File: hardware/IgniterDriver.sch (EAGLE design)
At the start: 22 parts, among them IC1 ATMEGA48/88/168-AU, Q1 FDD4141TO252, Q2 IRLML5203, Q4 16MHz, U2 MCP25625-E/SS

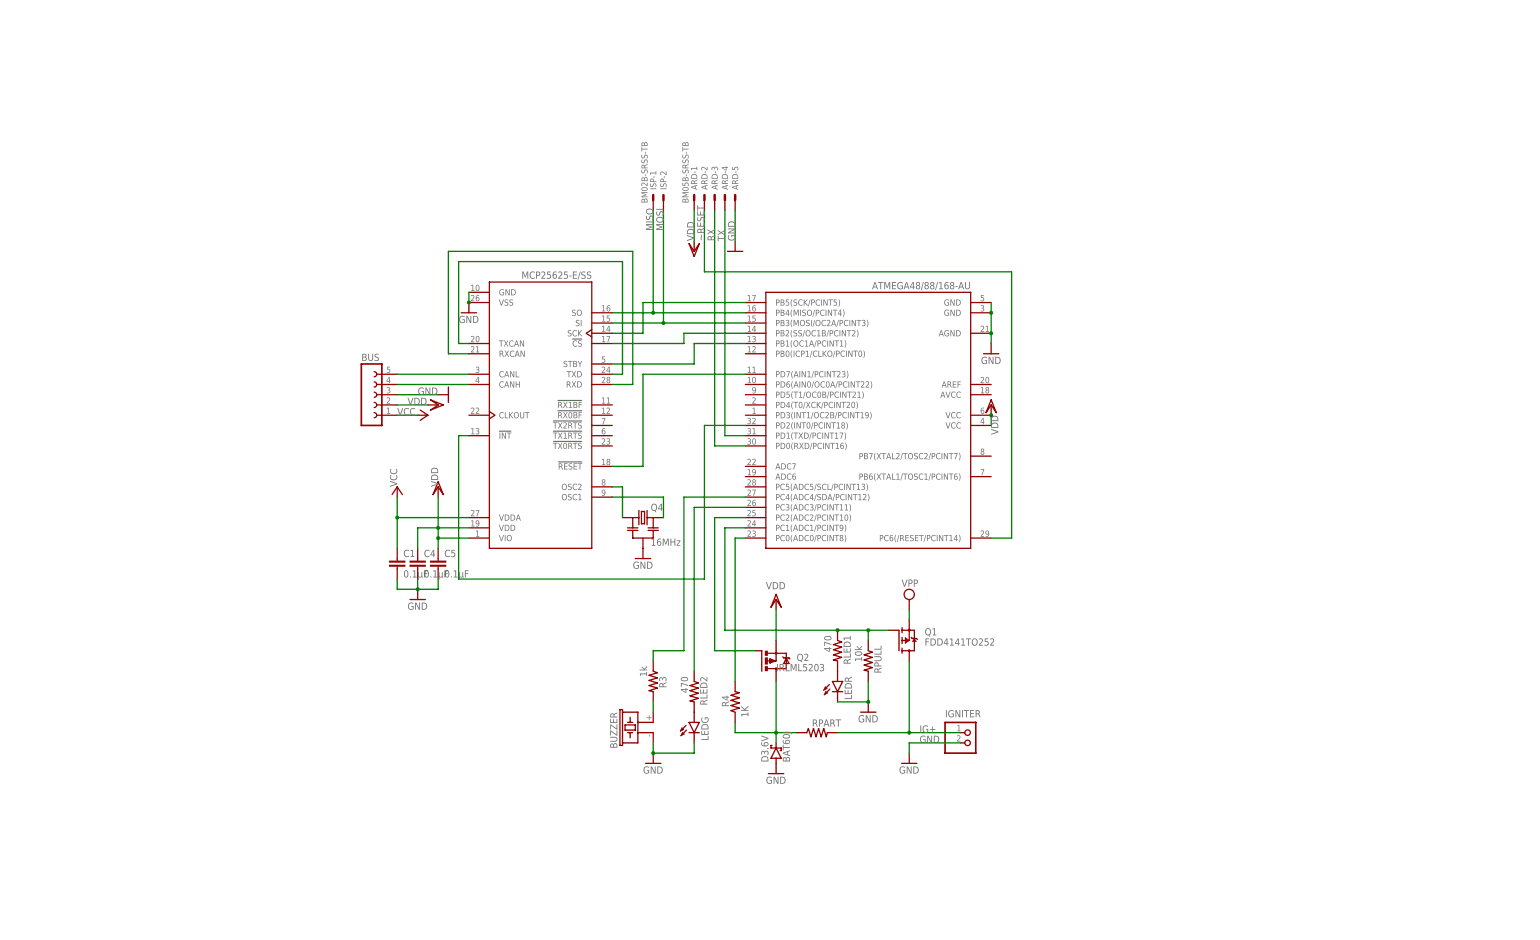
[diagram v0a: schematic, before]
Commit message: Add igniter driver board
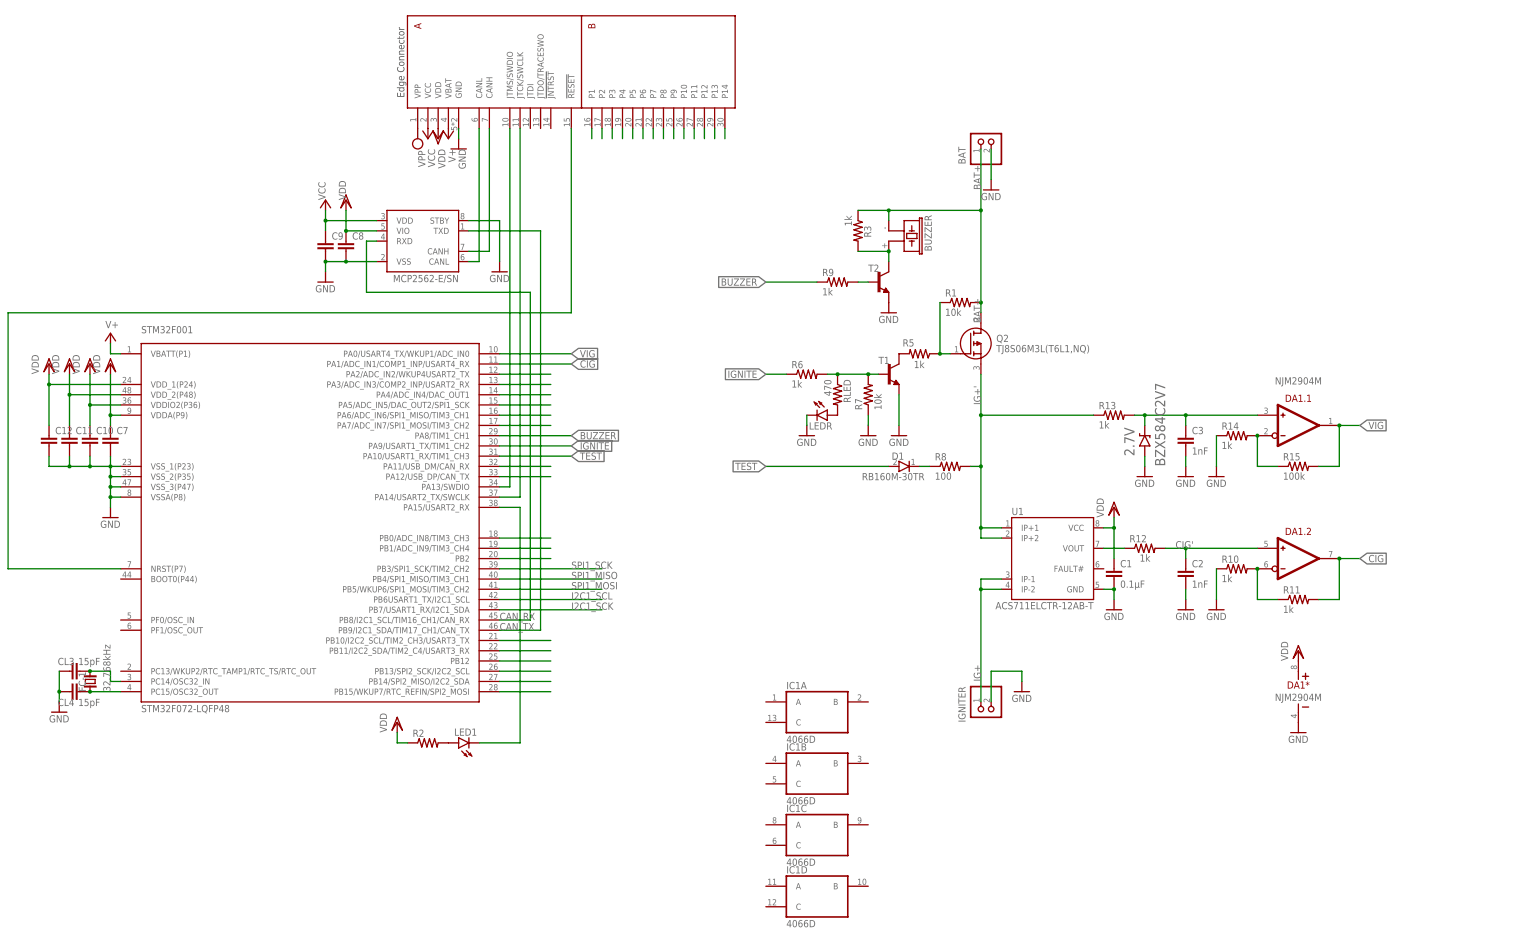
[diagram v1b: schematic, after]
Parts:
- removed ARD: BM05B-SRSS-TB, con-jst2:BM05B-SRSS-TB
- removed BUS: (no value), con-lsta:FE05-1
- removed C4, C5: 0.1μF, rcl:C-EUC0603
- removed D3.6V: BAT60J, diode:BAT60J
- removed ISP: BM02B-SRSS-TB, con-jst2:BM02B-SRSS-TB
- removed LEDG: (no value), led:LEDCHIPLED_0603
- removed Q1: FDD4141TO252, transistor-fet:FDD4141TO252
- removed Q4: 16MHz, m-pad-2.1:RESONATOR-MURATACST_CE
- removed R4: 1K, rcl:R-US_R0603
- removed RLED1, RLED2: 470, rcl:R-US_R0603
- removed RPART: (no value), rcl:R-US_R0603
- removed RPULL: 10k, rcl:R-US_R0603
- removed U2: MCP25625-E/SS, mcp25625-E_SS:MCP25625-E/SS
- added 2.7V: BZX584C2V7, diodes:BZX584C
- added BAT: (no value), con-jst-xh:S2B-XH-A
- added C10, C11, C12, C7, C8, C9: (no value), rcl:C-EUC0603K
- added C2, C3: 1nF, rcl:C-EUC0603K
- added CL3, CL4: 15pF, rcl:C-EUC0603K
- added D1: RB160M-30TR, RB160M-30TR:RB160M-30TR
- added DA1: NJM2904M, ic-jrc:NJM2904M
- added FC-1: 32.768kHz, crystal':CRYTALFC-255
- added LED1: (no value), led:LEDCHIP-LED0603
- added MCP1: MCP2562-E/SN, mcp2562-E_SN:MCP2562-E/SN
- added R1, R7: 10k, rcl:R-US_R0603
- added R10, R11, R12, R13, R14, R5, R6, R9: 1k, rcl:R-US_R0603
- added R15: 100k, rcl:R-US_R0603
- added R2: (no value), rcl:R-US_R0603
- added R8: 100, rcl:R-US_R0603
- added RLED: 470, rcl:R-US_R0603
- added STM32F001: STM32F072-LQFP48, stm32f0:STM32F072-LQFP48
- added T1, T2: (no value), transistor:-NPN-SOT23-EBC
- added U$2: EDGE30, bus:EDGE30
- added U1: ACS711ELCTR-12AB-T, allegro:ACS711ELCTR-12AB-T
- C1: value 0.1μF -> 0.1µF; device rcl:C-EUC0603 -> rcl:C-EUC0603K
- IC1: value ATMEGA48/88/168-AU -> 4066D; device atmega8:ATMEGA48/88/168-AU -> 40xx:4066D
- Q2: value IRLML5203 -> TJ8S06M3L(T6L1,NQ); device transistor-power:IRLML5203 -> TJ8S06M3L(T6L1_NQ):TJ8S06M3L(T6L1,NQ)
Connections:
- removed net MISO: IC1.PB4(MISO/PCINT4), ISP-1.S, U2.SO
- removed net MOSI: IC1.PB3(MOSI/OC2A/PCINT3), ISP-2.S, U2.SI
- removed net N$10: U2.TXCAN, U2.TXD
- removed net N$14: IC1.PC4(ADC4/SDA/PCINT12), R3.1
- removed net N$18: IC1.PD2(INT0/PCINT18), U2.!INT
- removed net N$26: IC1.PB2(SS/OC1B/PCINT2), U2.!CS
- removed net N$27: Q4.1, U2.OSC2
- removed net N$28: Q4.3, U2.OSC1
- removed net N$29: IC1.PB1(OC1A/PCINT1), U2.STBY
- removed net N$3: D3.6V.C, Q2.D, R4.1, RPART.1
- removed net N$30: IC1.PD7(AIN1/PCINT23), U2.!RESET
- removed net N$4: IC1.PC2(ADC2/PCINT10), Q2.G
- removed net N$5: LEDR.A, RLED1.2
- removed net RX: ARD-3.S, IC1.PD0(RXD/PCINT16)
- removed net TX: ARD-4.S, IC1.PD1(TXD/PCINT17)
- removed net ~RESET: ARD-2.S, IC1.PC6(/RESET/PCINT14)
- new net BAT+: BAT.1, BUZZER.2, Q2.D, R1.2, R3.1
- new net BUZZER: R9.1, STM32F001.PA8/TIM1_CH1
- new net CANH1: MCP1.CANH, U$2.CANH
- new net CANL1: MCP1.CANL, U$2.CANL
- new net CAN_RX: MCP1.RXD, STM32F001.PB8/I2C1_SCL/TIM16_CH1/CAN_RX
- new net CAN_TX: MCP1.TXD, STM32F001.PB9/I2C1_SDA/TIM17_CH1/CAN_TX
- new net CIG: DA1.2.OUT, R11.2, STM32F001.PA1/ADC_IN1/COMP1_INP/USART4_RX
- new net CIG': C2.1, DA1.2.IN+, R12.2
- new net I2C1_SCK: STM32F001.PB7/USART1_RX/I2C1_SDA
- new net I2C1_SCL: STM32F001.PB6USART1_TX/I2C1_SCL
- new net IG+': Q2.S, R13.1, R8.2, U1.IP+1, U1.IP+2
- new net IGNITE: R6.1, STM32F001.PA9/USART1_TX/TIM1_CH2
- new net N$15: R9.2, T2.B
- new net N$17: 2.7V.C, C3.1, DA1.1.IN+, R13.2
- new net N$46: U$2.P14
- new net N$47: U$2.P13
- new net N$48: U$2.P12
- new net N$49: U$2.P11
- new net N$50: U$2.P10
- new net N$51: U$2.P9
- new net N$52: U$2.P8
- new net N$53: U$2.P7
- new net N$54: U$2.P6
- new net N$55: U$2.P5
- new net N$56: U$2.P4
- new net N$57: U$2.P3
- new net N$60: STM32F001.PA2/ADC_IN2/WKUP4USART2_TX
- new net N$61: STM32F001.PA3/ADC_IN3/COMP2_INP/USART2_RX
- new net N$62: STM32F001.PA4/ADC_IN4/DAC_OUT1
- new net N$63: STM32F001.PA5/ADC_IN5/DAC_OUT2/SPI1_SCK
- new net N$64: STM32F001.PA6/ADC_IN6/SPI1_MISO/TIM3_CH1
- new net N$65: STM32F001.PA7/ADC_IN7/SPI1_MOSI/TIM3_CH2
- new net N$67: STM32F001.PA11/USB_DM/CAN_RX
- new net N$68: STM32F001.PA12/USB_DP/CAN_TX
- new net N$69: STM32F001.PB0/ADC_IN8/TIM3_CH3
- new net N$70: STM32F001.PB1/ADC_IN9/TIM3_CH4
- new net N$71: STM32F001.PB2
- new net N$72: STM32F001.PB10/I2C2_SCL/TIM2_CH3/USART3_TX
- new net N$73: STM32F001.PB11/I2C2_SDA/TIM2_C4/USART3_RX
- new net N$74: STM32F001.PB12
- new net N$75: STM32F001.PB13/SPI2_SCK/I2C2_SCL
- new net N$76: STM32F001.PB14/SPI2_MISO/I2C2_SDA
- new net N$77: STM32F001.PB15/WKUP7/RTC_REFIN/SPI2_MOSI
- new net N$78: CL4.2, FC-1.1, STM32F001.PC15/OSC32_OUT
- new net N$79: CL3.2, FC-1.2, STM32F001.PC14/OSC32_IN
- new net N$80: LED1.C, STM32F001.PA15/USART2_RX
- new net N$81: U$2.P1
- new net N$82: U$2.P2
- new net N$83: LED1.A, R2.2
- new net NRST1: STM32F001.NRST(P7), U$2.!RESET!
- new net SPI1_MISO: STM32F001.PB4/SPI1_MISO/TIM3_CH1
- new net SPI1_MOSI: STM32F001.PB5/WKUP6/SPI1_MOSI/TIM3_CH2
- new net SPI1_SCK: STM32F001.PB3/SPI1_SCK/TIM2_CH2
- new net SWCLK1: STM32F001.PA14/USART2_TX/SWCLK, U$2.JTCK/SWCLK
- new net SWDIO1: STM32F001.PA13/SWDIO, U$2.JTMS/SWDIO
- new net TEST: D1.A, STM32F001.PA10/USART1_RX/TIM1_CH3
- new net VBAT: STM32F001.VBATT(P1), U$2.VBAT
- new net VIG: DA1.1.OUT, R15.2, STM32F001.PA0/USART4_TX/WKUP1/ADC_IN0
- net GND: now also 2.7V.A, BAT.2, C10.2, C11.2, C12.2, C2.2, C3.2, C7.2, C8.2, C9.2, CL3.1, CL4.1, DA1*.V-, MCP1.STBY, MCP1.VSS, R10.1, R14.1, R7.1, STM32F001.VSSA(P8), STM32F001.VSS_1(P23), STM32F001.VSS_2(P35), STM32F001.VSS_3(P47), T1.E, T2.E, U$2.GND, U1.GND; no longer ARD-5.S, BUS.3, BUZZER.2, C4.2, C5.2, D3.6V.A, IC1.AGND, IC1.GND@1, IC1.GND@2, LEDG.C, Q4.2, RPULL.2, U2.GND, U2.VSS
- net IG+: now also U1.IP-1, U1.IP-2; no longer Q1.D, RPART.2
- net N$1: now also Q2.G, R1.1, R5.1; no longer IC1.PB5(SCK/PCINT5), U2.SCK
- net N$11: now also DA1.1.IN-, R14.2, R15.1; no longer U2.RXCAN, U2.RXD
- net N$12: now also DA1.2.IN-, R10.2, R11.1; no longer IC1.PC3(ADC3/PCINT11), RLED2.1
- net N$13: now also LEDR.A, RLED.2; no longer LEDG.A, RLED2.2
- net N$2: now also R5.2, T1.C; no longer IC1.PC0(ADC0/PCINT8), R4.2
- net N$6: now also R6.2, R7.2, RLED.1, T1.B; no longer IC1.PC1(ADC1/PCINT9), Q1.G, RLED1.1, RPULL.1
- net N$7: now also D1.K, R8.1; no longer BUS.5, U2.CANL
- net N$8: now also T2.C
- net N$9: now also R12.1, U1.VOUT; no longer BUS.4, U2.CANH
- net VCC: now also C9.1, MCP1.VDD, U$2.VCC; no longer BUS.1, C1.1, U2.VDDA
- net VDD: now also C1.1, C10.1, C11.1, C12.1, C7.1, C8.1, DA1*.V+, MCP1.VIO, R2.1, STM32F001.VDDA(P9), STM32F001.VDDIO2(P36), STM32F001.VDD_1(P24), STM32F001.VDD_2(P48), U$2.VDD, U1.VCC; no longer ARD-1.S, BUS.2, C4.1, C5.1, IC1.VCC@1, IC1.VCC@2, Q2.S, U2.VDD, U2.VIO
- net VPP: now also U$2.VPP; no longer Q1.S
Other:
- moved on the sheet: BUZZER, C1, IGNITER, LEDR, R3

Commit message: Layout igniter driver board
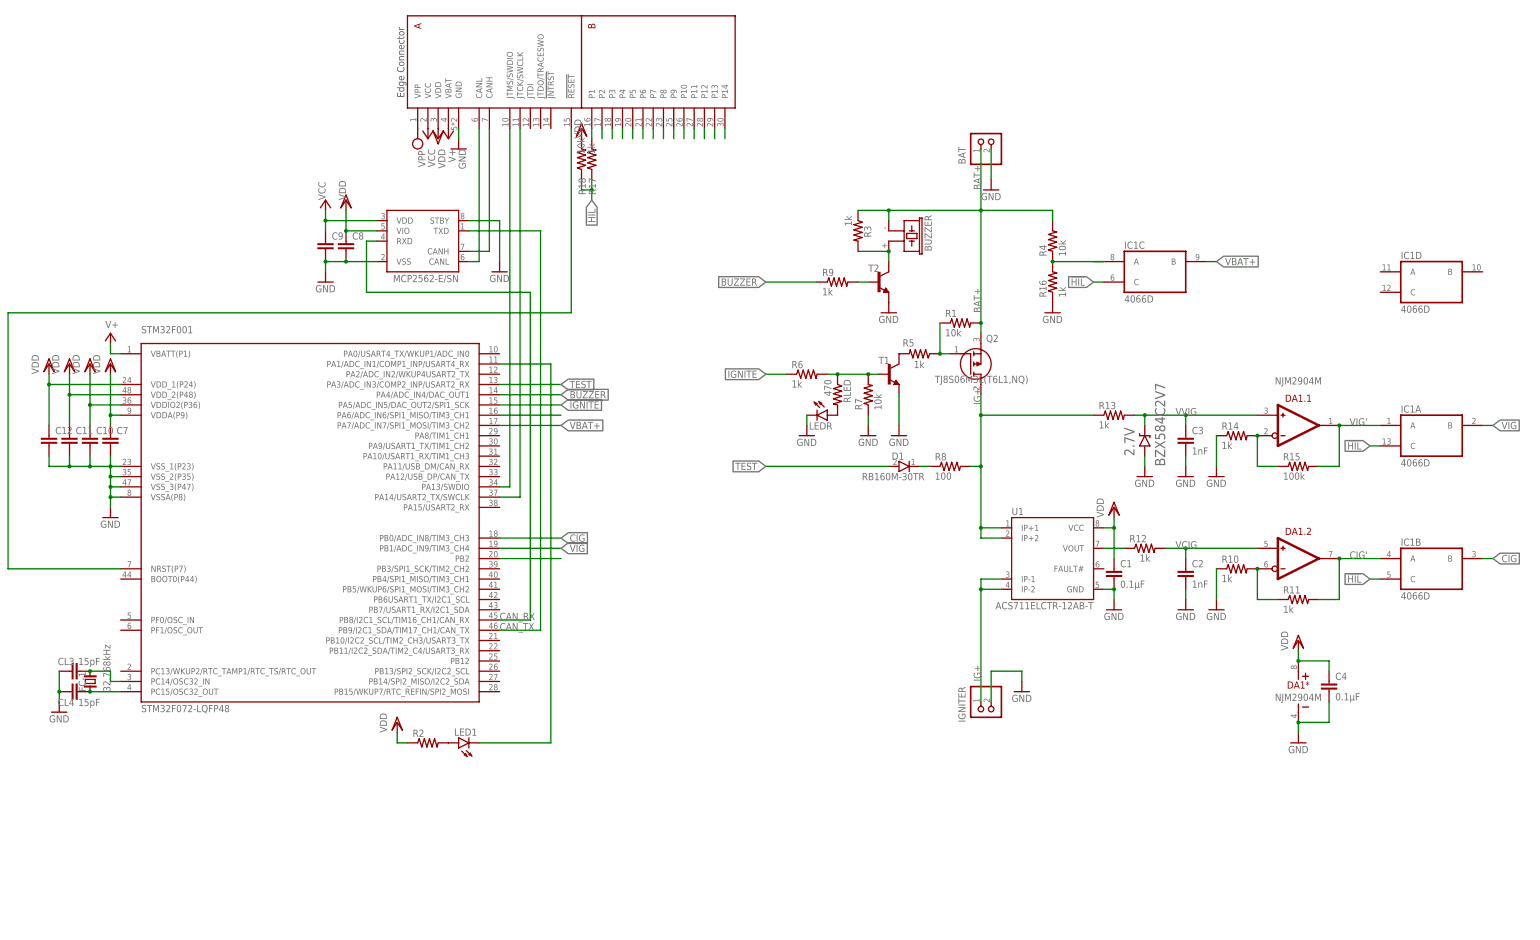
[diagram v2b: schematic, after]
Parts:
- added C4: 0.1µF, rcl:C-EUC0603K
- added R16, R17: 1k, rcl:R-US_R0603
- added R18, R4: 10k, rcl:R-US_R0603
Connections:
- net N$17 renamed VVIG
- net N$9 renamed VOUT
- removed net I2C1_SCK: STM32F001.PB7/USART1_RX/I2C1_SDA
- removed net I2C1_SCL: STM32F001.PB6USART1_TX/I2C1_SCL
- removed net N$60: STM32F001.PA2/ADC_IN2/WKUP4USART2_TX
- removed net N$61: STM32F001.PA3/ADC_IN3/COMP2_INP/USART2_RX
- removed net N$62: STM32F001.PA4/ADC_IN4/DAC_OUT1
- removed net N$63: STM32F001.PA5/ADC_IN5/DAC_OUT2/SPI1_SCK
- removed net N$65: STM32F001.PA7/ADC_IN7/SPI1_MOSI/TIM3_CH2
- removed net N$67: STM32F001.PA11/USB_DM/CAN_RX
- removed net N$68: STM32F001.PA12/USB_DP/CAN_TX
- removed net N$69: STM32F001.PB0/ADC_IN8/TIM3_CH3
- removed net N$70: STM32F001.PB1/ADC_IN9/TIM3_CH4
- removed net N$72: STM32F001.PB10/I2C2_SCL/TIM2_CH3/USART3_TX
- removed net N$73: STM32F001.PB11/I2C2_SDA/TIM2_C4/USART3_RX
- removed net N$74: STM32F001.PB12
- removed net N$75: STM32F001.PB13/SPI2_SCK/I2C2_SCL
- removed net N$76: STM32F001.PB14/SPI2_MISO/I2C2_SDA
- removed net N$77: STM32F001.PB15/WKUP7/RTC_REFIN/SPI2_MOSI
- removed net SPI1_MISO: STM32F001.PB4/SPI1_MISO/TIM3_CH1
- removed net SPI1_MOSI: STM32F001.PB5/WKUP6/SPI1_MOSI/TIM3_CH2
- removed net SPI1_SCK: STM32F001.PB3/SPI1_SCK/TIM2_CH2
- new net !HIL!: IC1A.C, IC1B.C, IC1C.C, R17.1, R18.1
- new net VBAT+: IC1C.B, STM32F001.PA7/ADC_IN7/SPI1_MOSI/TIM3_CH2
- new net VBAT+': IC1C.A, R16.2, R4.1
- new net VCIG: C2.1, DA1.2.IN+, R12.2
- new net VIG': DA1.1.OUT, IC1A.A, R15.2
- net BAT+: now also Q2.S, R4.2; no longer Q2.D
- net BUZZER: now also STM32F001.PA4/ADC_IN4/DAC_OUT1; no longer STM32F001.PA8/TIM1_CH1
- net CIG: now also IC1B.B, STM32F001.PB0/ADC_IN8/TIM3_CH3; no longer DA1.2.OUT, R11.2, STM32F001.PA1/ADC_IN1/COMP1_INP/USART4_RX
- net CIG': now also DA1.2.OUT, IC1B.A, R11.2; no longer C2.1, DA1.2.IN+, R12.2
- net GND: now also C4.2, R16.1
- net IG+': now also Q2.D; no longer Q2.S
- net IGNITE: now also STM32F001.PA5/ADC_IN5/DAC_OUT2/SPI1_SCK; no longer STM32F001.PA9/USART1_TX/TIM1_CH2
- net N$80: now also STM32F001.PA1/ADC_IN1/COMP1_INP/USART4_RX; no longer STM32F001.PA15/USART2_RX
- net N$81: now also R17.2
- net TEST: now also STM32F001.PA3/ADC_IN3/COMP2_INP/USART2_RX; no longer STM32F001.PA10/USART1_RX/TIM1_CH3
- net VDD: now also C4.1, R18.2
- net VIG: now also IC1A.B, STM32F001.PB1/ADC_IN9/TIM3_CH4; no longer DA1.1.OUT, R15.2, STM32F001.PA0/USART4_TX/WKUP1/ADC_IN0
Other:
- moved on the sheet: IC1A, IC1B, IC1C, IC1D, Q2, R1

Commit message: Complete igniter driver board
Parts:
- added R19, R20, R21: 1k, resistor:R-US_R0603
- renumbered 2.7V to D2, DA1 to OP, FC-1 to CRYSTAL, LED1 to LEDG, MCP1 to MCP2562, Q2 to T3, R2 to RLED2, RLED to RLED1, U1 to 1C2
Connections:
- net VBAT renamed VBU
- removed net N$46: U$2.P14
- removed net N$48: U$2.P12
- removed net N$49: U$2.P11
- removed net N$50: U$2.P10
- removed net N$51: U$2.P9
- removed net N$54: U$2.P6
- removed net N$55: U$2.P5
- removed net N$56: U$2.P4
- removed net N$57: U$2.P3
- removed net N$82: U$2.P2
- net BUZZER: now also U$2.P11
- net CIG: now also R19.1
- net IGNITE: now also U$2.P10
- net N$47: now also R21.2
- net N$52: now also R19.2
- net N$53: now also R20.2
- net TEST: now also U$2.P12
- net VBAT+: now also R21.1
- net VIG: now also R20.1
